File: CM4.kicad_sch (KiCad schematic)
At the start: 4 parts

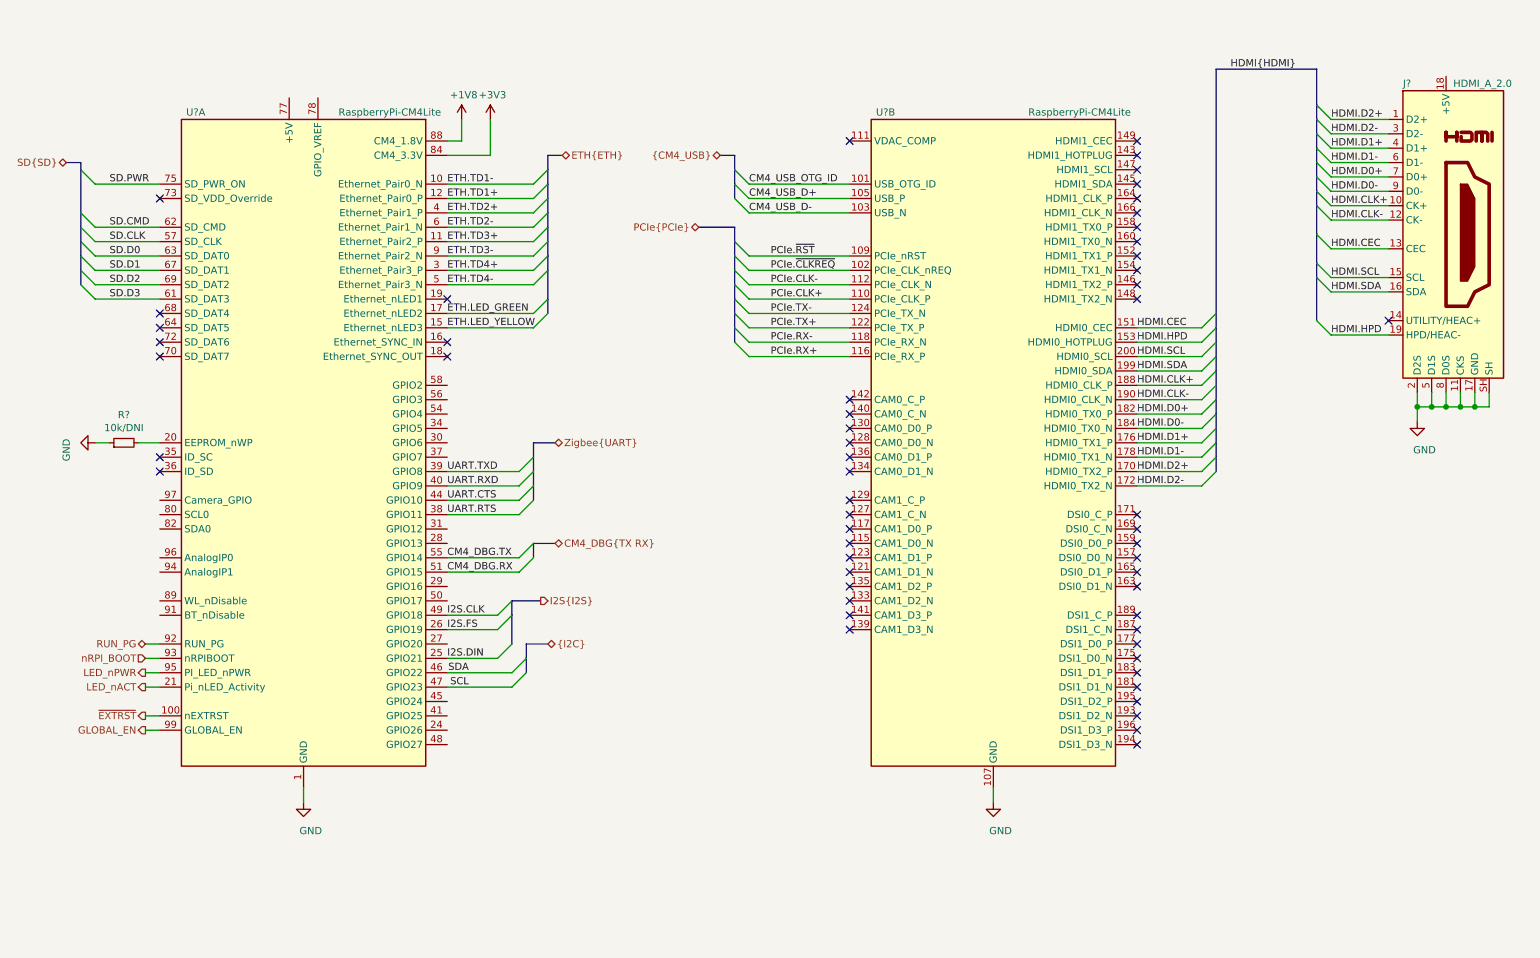
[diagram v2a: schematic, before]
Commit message: -Connected remaining nets -CM4 symbol fixups -Used single 6x OE buffer chip instead of 4x single -Added PWM FAN
Signed-off-by: Dominik Sliwa <dominik@sliwa.io>
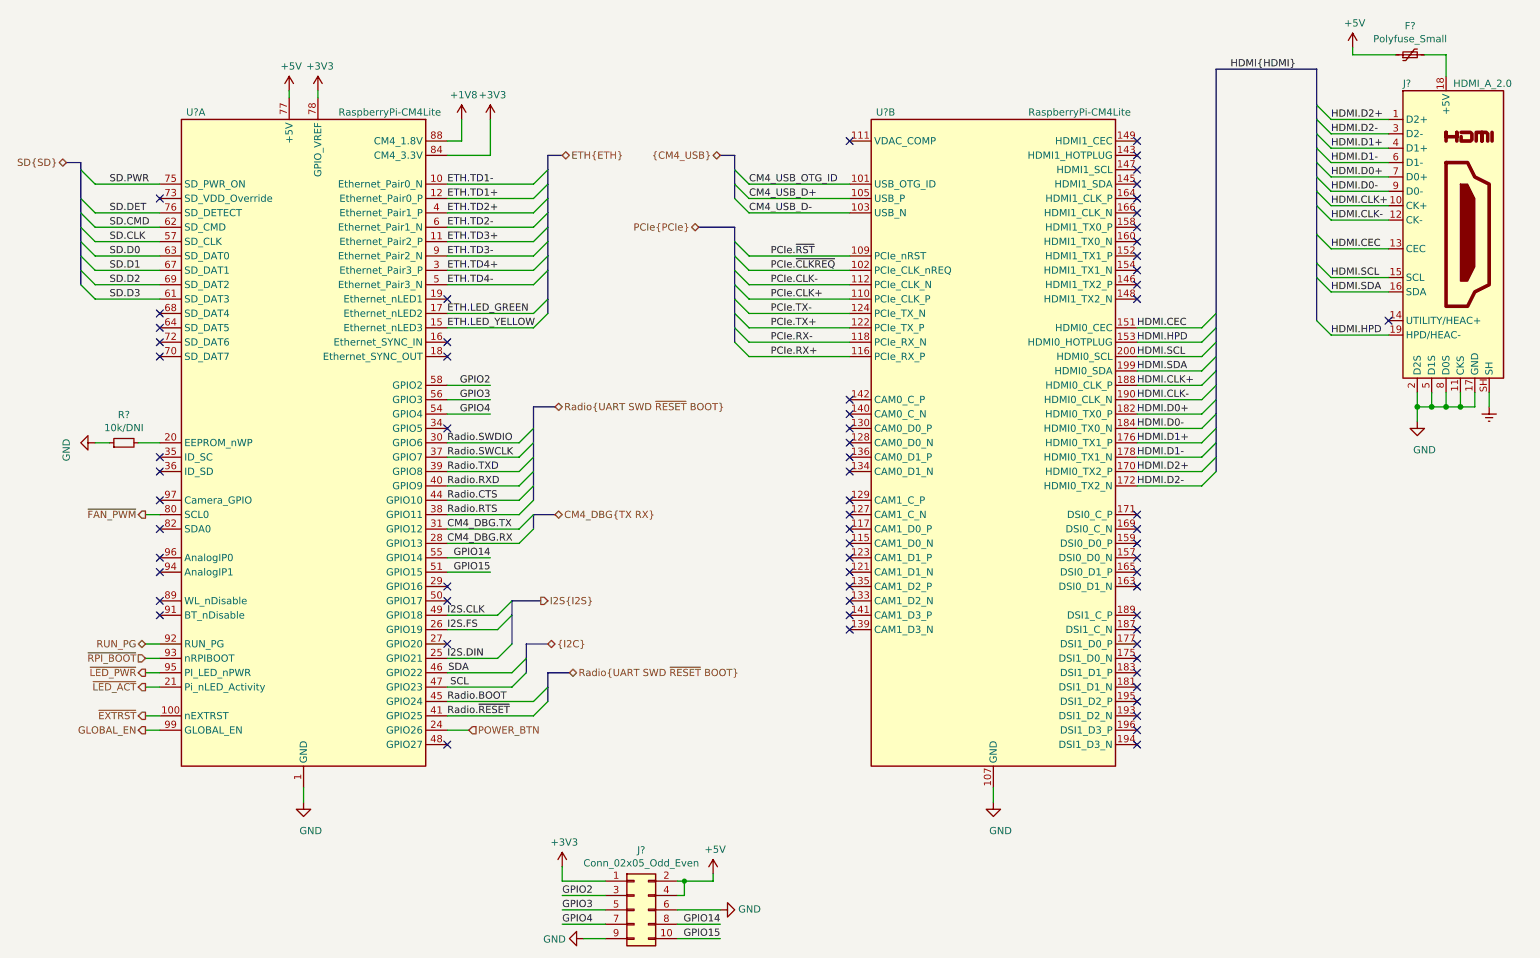
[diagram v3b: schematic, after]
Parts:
- added F?: Polyfuse_Small, symbol Device:Polyfuse_Small
- added J?: Conn_02x05_Odd_Even, symbol Connector_Generic:Conn_02x05_Odd_Even
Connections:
- net +3V3: now also U?.78 (GPIO_VREF), J?.1 (Pin_1)
- net CM4_DBG.RX: now also U?.28 (GPIO13); no longer U?.51 (GPIO15)
- net CM4_DBG.TX: now also U?.31 (GPIO12); no longer U?.55 (GPIO14)
- net GND: now also J?.6 (Pin_6), J?.9 (Pin_9); no longer J?.SH
- net POWER_BTN: now reaches U?.24 (GPIO26)
- net Radio.SWDIO: now reaches U?.30 (GPIO6)
- net Radio.SWCLK: now reaches U?.37 (GPIO7)
- net Radio.~RESET: now reaches U?.41 (GPIO25)
- net Radio.BOOT: now reaches U?.45 (GPIO24)
- net GPIO4: now reaches U?.54 (GPIO4)
- net GPIO4: now also J?.7 (Pin_7)
- net GPIO3: now reaches U?.56 (GPIO3)
- net GPIO3: now also J?.5 (Pin_5)
- net GPIO2: now reaches U?.58 (GPIO2)
- net GPIO2: now also J?.3 (Pin_3)
- net SD.DET: now reaches U?.76 (Reserved)
- net +5V: now reaches U?.77 (+5V), U?.79 (+5V), U?.81 (+5V), U?.83 (+5V), U?.85 (+5V), U?.87 (+5V)
- net +5V: now also F?.1, J?.2 (Pin_2), J?.4 (Pin_4)
- net ~FAN_PWM: now reaches U?.80 (SCL0)
- net at J?.18 (+5V): now also F?.2
- net LED_nACT renamed ~LED_ACT
- net LED_nPWR renamed ~LED_PWR
- net UART.CTS renamed Radio.CTS
- net UART.RTS renamed Radio.RTS
- net UART.RXD renamed Radio.RXD
- net UART.TXD renamed Radio.TXD
- net nRPI_BOOT renamed ~RPI_BOOT
- new net Earth: J?.SH
- new net GPIO14: J?.8 (Pin_8), U?.55 (GPIO14)
- new net GPIO15: J?.10 (Pin_10), U?.51 (GPIO15)
- no-connect marks 56 -> 67

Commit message: PoE and clean-up
- Moved PoE to a seperate sheet and finished design
- Started using Config field for Variants and DNP flag
- Fix-ups
- Added Wurth 749119550 and TI TPS23734 to the symbol library
- Changed RTC from PCF8563 to PCF85063

Signed-off-by: Dominik Sliwa <dominik@sliwa.io>
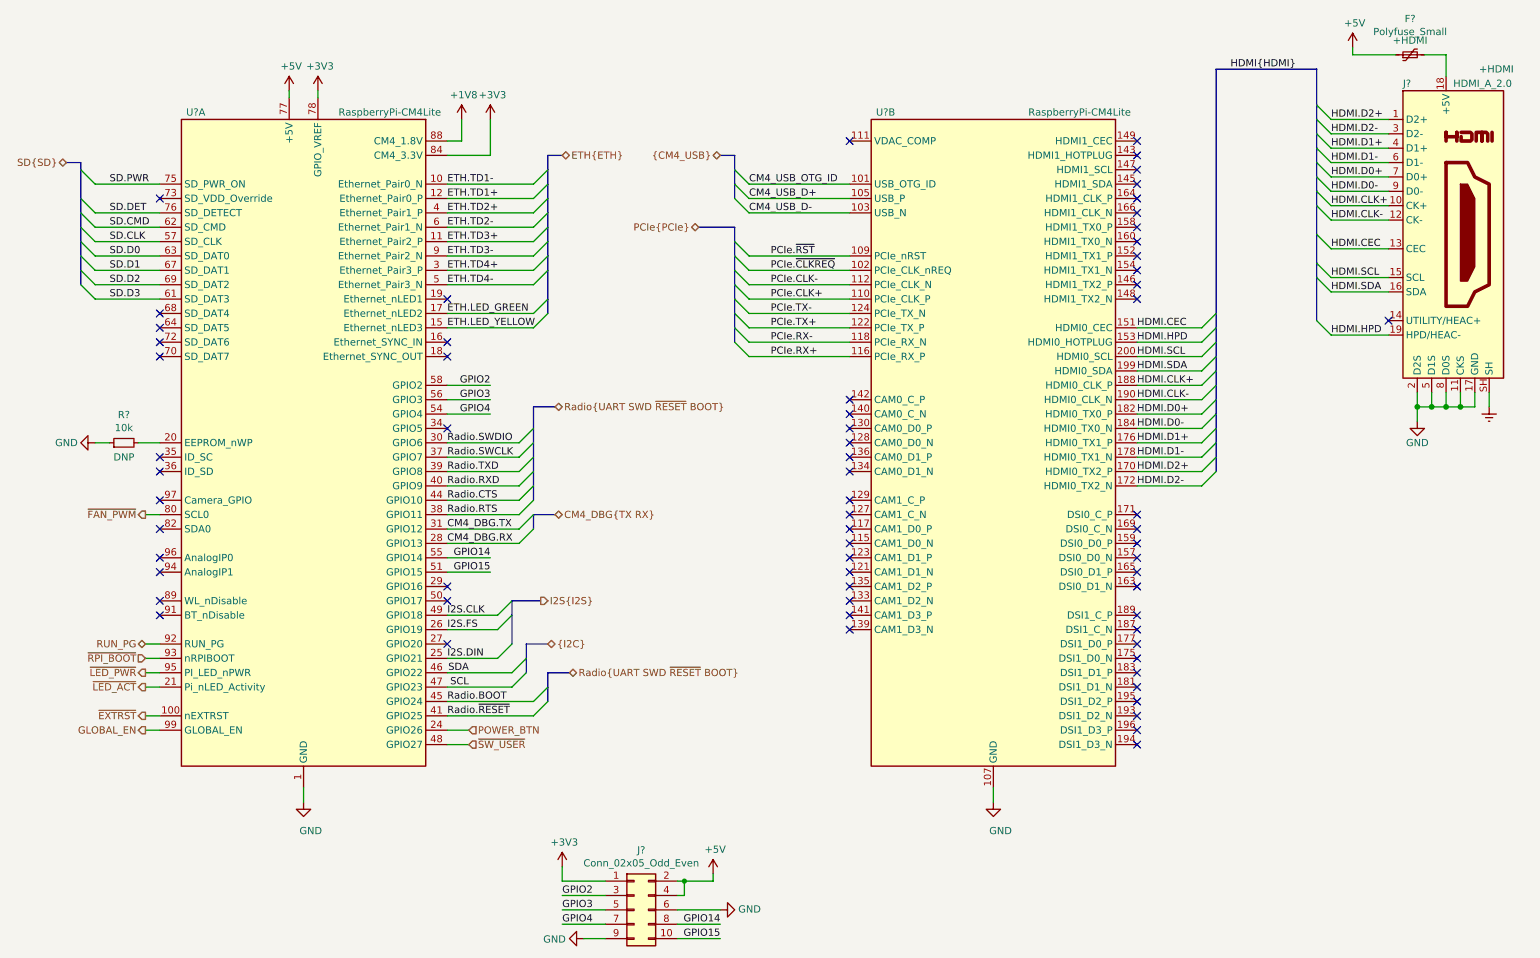
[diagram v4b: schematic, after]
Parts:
- F?, J?: Config (none) -> +HDMI
- R?: value 10k/DNI -> 10k; Config (none) -> DNP
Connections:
- net ~SW_USER: now reaches U?.48 (GPIO27)
- no-connect marks 67 -> 66
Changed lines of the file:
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@@
   (junction (at 265.43 82.55) (diameter 1.016) (color 0 0 0 0))
   (junction (at 267.97 82.55) (diameter 1.016) (color 0 0 0 0))
-  (no_connect (at 210.82 109.22))
-  (no_connect (at 160.02 86.36))
+  (no_connect (at 38.1 109.22))
+  (no_connect (at 38.1 45.72))
+  (no_connect (at 210.82 142.24))
+  (no_connect (at 160.02 101.6))
+  (no_connect (at 210.82 137.16))
+  (no_connect (at 210.82 43.18))
+  (no_connect (at 88.9 116.84))
+  (no_connect (at 88.9 63.5))
+  (no_connect (at 160.02 111.76))
+  (no_connect (at 210.82 114.3))
+  (no_connect (at 38.1 119.38))
   (no_connect (at 160.02 119.38))
-  (no_connect (at 160.02 93.98))
-  (no_connect (at 88.9 142.24))
+  (no_connect (at 210.82 127))
   (no_connect (at 210.82 104.14))
-  (no_connect (at 210.82 142.24))
-  (no_connect (at 210.82 127))
-  (no_connect (at 38.1 93.98))
-  (no_connect (at 210.82 132.08))
-  (no_connect (at 210.82 137.16))
-  (no_connect (at 38.1 104.14))
-  (no_connect (at 210.82 101.6))
-  (no_connect (at 88.9 71.12))
-  (no_connect (at 38.1 45.72))
-  (no_connect (at 210.82 35.56))
-  (no_connect (at 160.02 109.22))
-  (no_connect (at 160.02 114.3))
-  (no_connect (at 210.82 139.7))
+  (no_connect (at 160.02 106.68))
   (no_connect (at 210.82 134.62))
-  (no_connect (at 38.1 99.06))
-  (no_connect (at 160.02 106.68))
-  (no_connect (at 210.82 48.26))
-  (no_connect (at 210.82 121.92))
-  (no_connect (at 88.9 63.5))
-  (no_connect (at 160.02 101.6))
-  (no_connect (at 88.9 86.36))
-  (no_connect (at 210.82 40.64))
-  (no_connect (at 160.02 88.9))
+  (no_connect (at 38.1 71.12))
+  (no_connect (at 88.9 73.66))
+  (no_connect (at 210.82 55.88))
   (no_connect (at 160.02 91.44))
   (no_connect (at 210.82 53.34))
+  (no_connect (at 210.82 58.42))
+  (no_connect (at 210.82 106.68))
+  (no_connect (at 38.1 99.06))
+  (no_connect (at 38.1 91.44))
+  (no_connect (at 88.9 71.12))
+  (no_connect (at 210.82 101.6))
+  (no_connect (at 160.02 104.14))
+  (no_connect (at 160.02 114.3))
+  (no_connect (at 38.1 66.04))
+  (no_connect (at 210.82 129.54))
+  (no_connect (at 160.02 35.56))
+  (no_connect (at 38.1 73.66))
+  (no_connect (at 210.82 139.7))
+  (no_connect (at 38.1 93.98))
+  (no_connect (at 210.82 124.46))
+  (no_connect (at 210.82 35.56))
+  (no_connect (at 210.82 63.5))
+  (no_connect (at 160.02 109.22))
+  (no_connect (at 38.1 111.76))
+  (no_connect (at 210.82 60.96))
+  (no_connect (at 160.02 93.98))
+  (no_connect (at 255.27 67.31))
+  (no_connect (at 38.1 68.58))
+  (no_connect (at 210.82 40.64))
   (no_connect (at 210.82 50.8))
+  (no_connect (at 160.02 86.36))
+  (no_connect (at 160.02 88.9))
+  (no_connect (at 160.02 83.82))
+  (no_connect (at 88.9 124.46))
+  (no_connect (at 160.02 116.84))
+  (no_connect (at 38.1 104.14))
+  (no_connect (at 210.82 48.26))
+  (no_connect (at 210.82 132.08))
+  (no_connect (at 88.9 86.36))
+  (no_connect (at 210.82 45.72))
+  (no_connect (at 88.9 114.3))
+  (no_connect (at 210.82 111.76))
+  (no_connect (at 210.82 109.22))
   (no_connect (at 210.82 38.1))
-  (no_connect (at 38.1 73.66))
-  (no_connect (at 38.1 91.44))
-  (no_connect (at 160.02 104.14))
-  (no_connect (at 160.02 111.76))
+  (no_connect (at 160.02 81.28))
+  (no_connect (at 160.02 121.92))
+  (no_connect (at 160.02 99.06))
+  (no_connect (at 210.82 119.38))
   (no_connect (at 38.1 116.84))
-  (no_connect (at 38.1 71.12))
-  (no_connect (at 210.82 111.76))
-  (no_connect (at 160.02 99.06))
-  (no_connect (at 38.1 68.58))
-  (no_connect (at 210.82 129.54))
-  (no_connect (at 210.82 119.38))
-  (no_connect (at 210.82 63.5))
-  (no_connect (at 210.82 45.72))
-  (no_connect (at 38.1 111.76))
-  (no_connect (at 88.9 114.3))
-  (no_connect (at 88.9 116.84))
-  (no_connect (at 88.9 124.46))
-  (no_connect (at 38.1 66.04))
-  (no_connect (at 210.82 114.3))
-  (no_connect (at 210.82 106.68))
-  (no_connect (at 255.27 67.31))
-  (no_connect (at 210.82 124.46))
-  (no_connect (at 38.1 109.22))
-  (no_connect (at 210.82 55.88))
-  (no_connect (at 160.02 35.56))
-  (no_connect (at 210.82 58.42))
-  (no_connect (at 160.02 121.92))
-  (no_connect (at 88.9 73.66))
-  (no_connect (at 160.02 83.82))
-  (no_connect (at 160.02 116.84))
-  (no_connect (at 38.1 119.38))
-  (no_connect (at 210.82 60.96))
-  (no_connect (at 160.02 81.28))
-  (no_connect (at 210.82 43.18))
+  (no_connect (at 210.82 121.92))
   (bus_entry (at 24.13 40.64) (size 2.54 2.54)
     (stroke (width 0.1524) (type solid) (color 0 0 0 0))
@@
   )
   (wire (pts (xy 88.9 139.7) (xy 92.71 139.7))
+    (stroke (width 0) (type solid) (color 0 0 0 0))
+  )
+  (wire (pts (xy 88.9 142.24) (xy 92.71 142.24))
     (stroke (width 0) (type solid) (color 0 0 0 0))
   )
@@
     (effects (font (size 1.27 1.27)) (justify left))
   )
+  (hierarchical_label "~SW_USER" (shape input) (at 92.71 142.24 0)
+    (effects (font (size 1.27 1.27)) (justify left))
+  )
   (hierarchical_label "I2S{I2S}" (shape output) (at 105.41 116.84 0)
     (effects (font (size 1.27 1.27)) (justify left))
@@
       (effects (font (size 1.27 1.27)) hide)
     )
-    (property "Value" "GND" (id 1) (at 21.59 90.17 0))
+    (property "Value" "GND" (id 1) (at 21.59 88.9 90))
     (property "Footprint" "" (id 2) (at 26.67 88.9 0)
       (effects (font (size 1.27 1.27)) hide)
@@
       (effects (font (size 1.27 1.27)) hide)
     )
-    (property "Value" "GND" (id 1) (at 261.62 90.17 0))
+    (property "Value" "GND" (id 1) (at 260.35 88.9 0))
     (property "Footprint" "" (id 2) (at 260.35 85.09 0)
       (effects (font (size 1.27 1.27)) hide)
@@
     (in_bom yes) (on_board yes)
     (property "Reference" "R?" (id 0) (at 31.75 83.9532 90))
-    (property "Value" "10k/DNI" (id 1) (at 31.75 86.252 90))
+    (property "Value" "10k" (id 1) (at 31.75 86.252 90))
     (property "Footprint" "" (id 2) (at 31.75 88.9 0)
       (effects (font (size 1.27 1.27)) hide)
@@
       (effects (font (size 1.27 1.27)) hide)
     )
+    (property "Config" "DNP" (id 4) (at 31.75 91.44 90))
   )
   (symbol (lib_id "Device:Polyfuse_Small") (at 259.08 20.32 90) (unit 1)
     (in_bom yes) (on_board yes)
-    (property "Reference" "F?" (id 0) (at 259.08 15.2208 90))
-    (property "Value" "Polyfuse_Small" (id 1) (at 259.08 17.5195 90))
+    (property "Reference" "F?" (id 0) (at 259.08 13.9508 90))
+    (property "Value" "Polyfuse_Small" (id 1) (at 259.08 16.2495 90))
     (property "Footprint" "" (id 2) (at 264.16 19.05 0)
       (effects (font (size 1.27 1.27)) (justify left) hide)
@@
       (effects (font (size 1.27 1.27)) hide)
     )
+    (property "Config" "+HDMI" (id 4) (at 259.08 17.78 90))
   )
   (symbol (lib_id "Connector_Generic:Conn_02x05_Odd_Even") (at 121.92 171.45 0) (unit 1)
@@
       (effects (font (size 1.27 1.27)) hide)
     )
+    (property "Config" "+HDMI" (id 4) (at 274.32 22.86 0))
   )
   (symbol (lib_name "LightBlue:RaspberryPi-CM4Lite_1") (lib_id "LightBlue:RaspberryPi-CM4Lite") (at 185.42 88.9 0) (unit 2)

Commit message: Annotate symbools and assign capacitor footprints
Signed-off-by: Stefan Agner <stefan@agner.ch>
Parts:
- gave numbers to parts that had none: 5
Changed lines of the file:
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@@
   (symbol (lib_id "Device:R_Small") (at 31.75 88.9 90) (unit 1)
     (in_bom yes) (on_board yes)
-    (property "Reference" "R?" (id 0) (at 31.75 83.9532 90))
+    (property "Reference" "R1" (id 0) (at 31.75 83.9532 90))
     (property "Value" "10k" (id 1) (at 31.75 86.252 90))
     (property "Footprint" "" (id 2) (at 31.75 88.9 0)
@@
   (symbol (lib_id "Device:Polyfuse_Small") (at 259.08 20.32 90) (unit 1)
     (in_bom yes) (on_board yes)
-    (property "Reference" "F?" (id 0) (at 259.08 13.9508 90))
+    (property "Reference" "F1" (id 0) (at 259.08 13.9508 90))
     (property "Value" "Polyfuse_Small" (id 1) (at 259.08 16.2495 90))
     (property "Footprint" "" (id 2) (at 264.16 19.05 0)
@@
   (symbol (lib_id "Connector_Generic:Conn_02x05_Odd_Even") (at 121.92 171.45 0) (unit 1)
     (in_bom yes) (on_board yes)
-    (property "Reference" "J?" (id 0) (at 123.19 160.8898 0))
+    (property "Reference" "J1" (id 0) (at 123.19 160.8898 0))
     (property "Value" "Conn_02x05_Odd_Even" (id 1) (at 123.19 163.1885 0))
     (property "Footprint" "" (id 2) (at 121.92 171.45 0)
@@
   (symbol (lib_id "Connector:HDMI_A_1.4") (at 265.43 52.07 0) (unit 1)
     (in_bom yes) (on_board yes)
-    (property "Reference" "J?" (id 0) (at 257.81 25.4 0)
+    (property "Reference" "J2" (id 0) (at 257.81 25.4 0)
       (effects (font (size 1.27 1.27)) (justify left))
     )
@@
   (symbol (lib_name "LightBlue:RaspberryPi-CM4Lite_1") (lib_id "LightBlue:RaspberryPi-CM4Lite") (at 185.42 88.9 0) (unit 2)
     (in_bom yes) (on_board yes)
-    (property "Reference" "U?" (id 0) (at 166.37 30.48 0))
+    (property "Reference" "U1" (id 0) (at 166.37 30.48 0))
     (property "Value" "RaspberryPi-CM4Lite" (id 1) (at 200.66 30.48 0))
     (property "Footprint" "Module:RaspberryPi-CM4" (id 2) (at 198.12 147.32 0)
@@
   (symbol (lib_id "LightBlue:RaspberryPi-CM4Lite") (at 63.5 88.9 0) (unit 1)
     (in_bom yes) (on_board yes)
-    (property "Reference" "U?" (id 0) (at 44.45 30.48 0))
+    (property "Reference" "U1" (id 0) (at 44.45 30.48 0))
     (property "Value" "RaspberryPi-CM4Lite" (id 1) (at 78.74 30.48 0))
     (property "Footprint" "Module:RaspberryPi-CM4" (id 2) (at 76.2 147.32 0)
